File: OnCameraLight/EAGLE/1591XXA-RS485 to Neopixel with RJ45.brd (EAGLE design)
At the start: 54 x 29 mm, 8 parts, among them IC1 75176AP, J1 RJHSE-5381

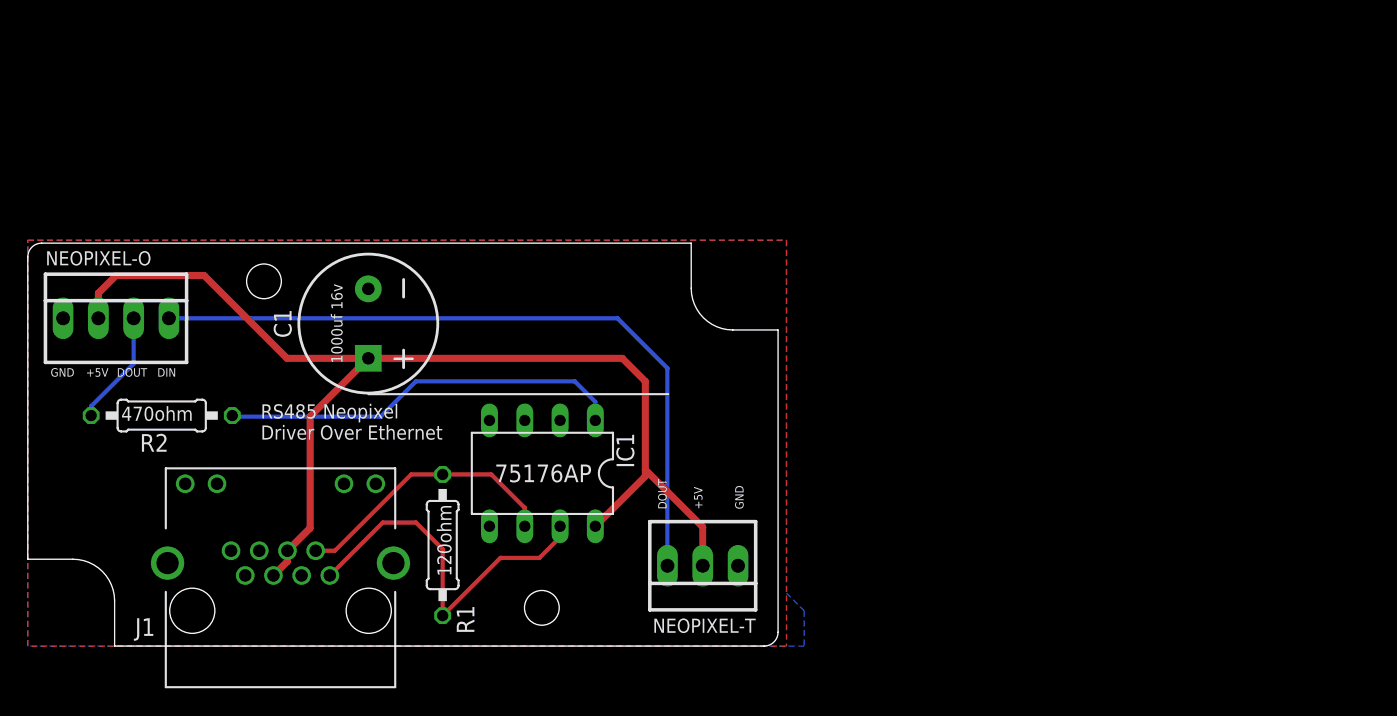
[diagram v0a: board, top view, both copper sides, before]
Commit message: Some more designs to fit different Hammond enclosures.
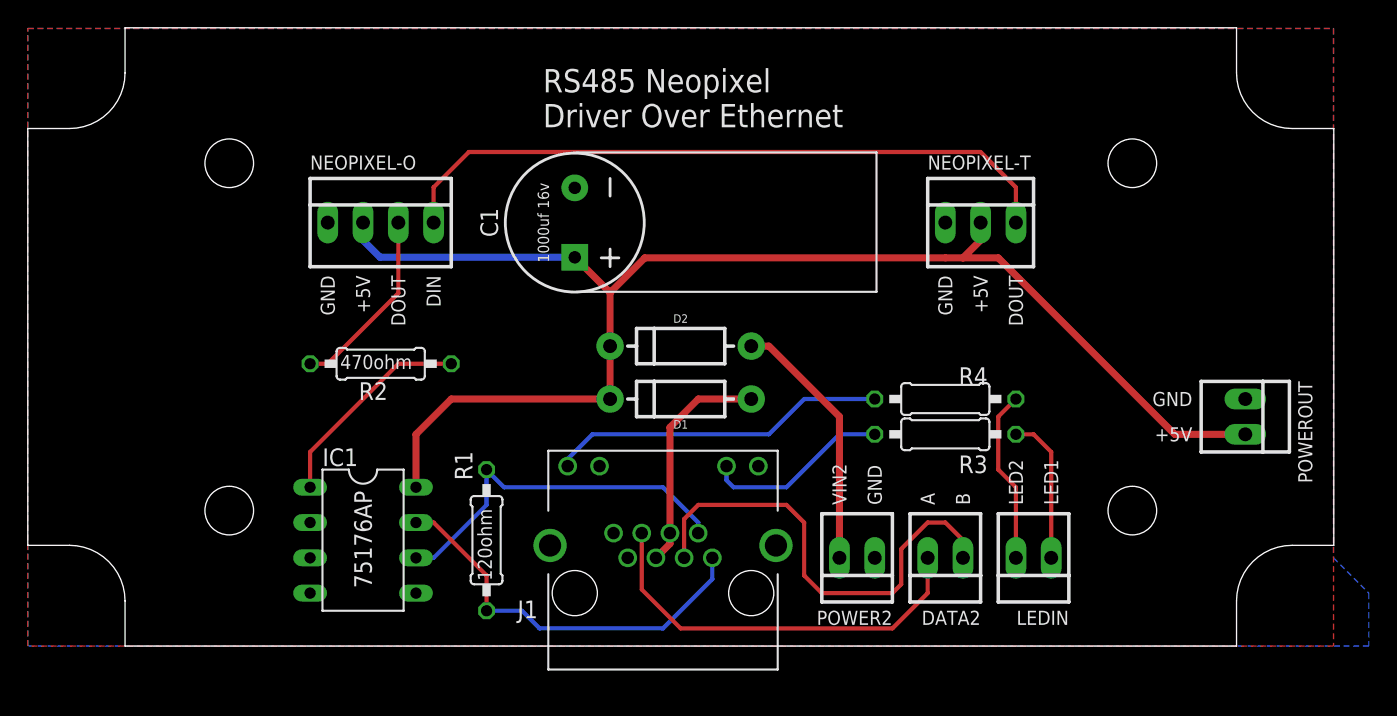
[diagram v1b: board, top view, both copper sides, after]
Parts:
- added D1, D2: 1A/50V/1.1V, SparkFun-DiscreteSemi:DIODE-1N4001
- added DATA2, LEDIN, POWER2, POWEROUT: 22-23-2021, con-molex:22-23-2021
- added R3, R4: (no value), rcl:0207/10
- BOX1: value HAMMOND-BOX-1551H -> HAMMOND-BOX-1591XXA; device hammond:1551H -> hammond:1591XXA
- moved NEOPIXEL-T 31.8 mm to (68.6, 30.5), turned to 0 degrees
- moved J1 27.6 mm to (45.7, 3.81)
- moved NEOPIXEL-O 20.3 mm to (25.4, 30.5)
- moved C1 16.5 mm to (39.4, 30.5)
- moved R2 16.2 mm to (25.4, 20.3)
- moved IC1 13.8 mm to (24.1, 7.62), turned to 270 degrees
- moved R1 3.18 mm to (33.0, 7.62), turned to 270 degrees
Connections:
- removed net DATA2+: J1.3
- removed net DATA2-: J1.6
- removed net RS485+: IC1.7, J1.1, R1.1
- removed net RS485-: IC1.6, J1.2, R1.2
- new net DATA1A: IC1.6, J1.2, R1.1
- new net DATA1B: IC1.7, J1.1, R1.2
- new net DATA2A: DATA2.2, J1.6
- new net DATA2B: DATA2.1, J1.3
- new net LED1IN: LEDIN.1, R3.1
- new net LED2IN: LEDIN.2, R4.1
- new net VIN1: D1.A, J1.4, J1.5
- new net VIN2: D2.A, POWER2.2
- net GND: now also POWER2.1, POWEROUT.1
- net LED1: now also R3.2
- net LED2: now also R4.2
- net VCC: now also D1.C, D2.C, POWEROUT.2; no longer J1.4, J1.5
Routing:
- net DATA2B: track 0.00 -> 33.5 mm
- net DATA2A: track 0.00 -> 29.4 mm
- net DATA1B: track 0.00 -> 29.0 mm
- net RS485+: track 26.8 -> 0.00 mm
- net DATA1A: track 0.00 -> 26.8 mm
- net LED2: track 0.00 -> 24.4 mm
- net RS485-: track 19.6 -> 0.00 mm
- net VIN2: track 0.00 -> 18.6 mm
- net VCC: track 83.9 -> 102.2 mm
- net VIN1: track 0.00 -> 16.5 mm
- net NEODATA: track 29.2 -> 15.3 mm
- net LED1: track 0.00 -> 13.5 mm
- net LED2IN: track 0.00 -> 12.5 mm
- net LED1IN: track 0.00 -> 10.7 mm
- net NEO-O: track 8.27 -> 13.5 mm
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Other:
- board size 54 x 29 mm -> 94 x 44.5 mm
- board text added: "A"
- board text added: "B"
- board text added: "Fits Hammond 1591XXA"
- board text added: "LED1"
- board text added: "LED2"
- board text added: "VIN2"
- board text removed: "Fits Hammond 1551H"

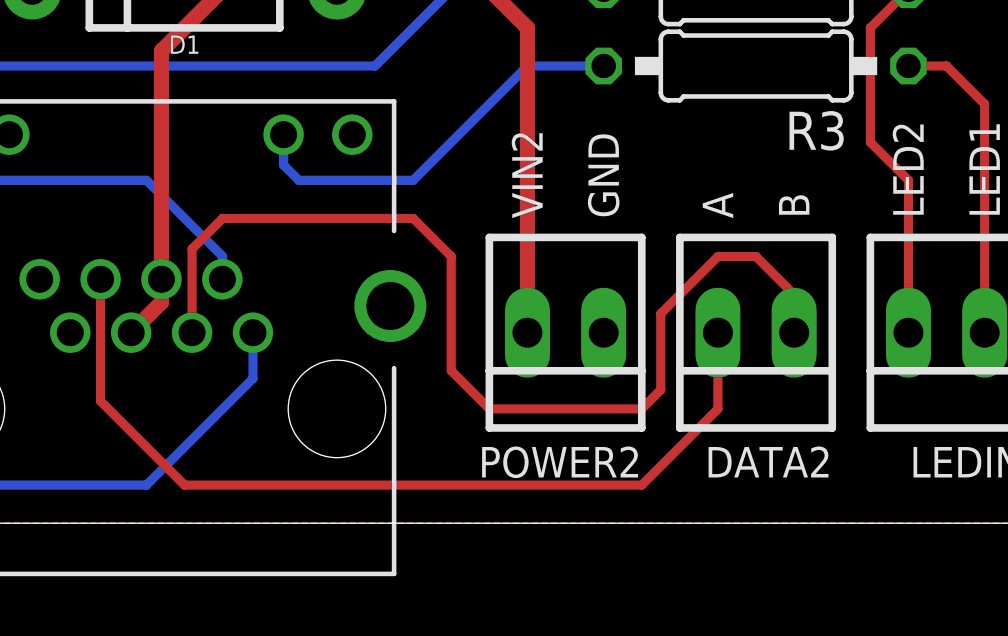
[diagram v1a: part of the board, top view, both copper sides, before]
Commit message: Go through and fix notation on RS485 wiring everywhere to use the standard A/B notation.
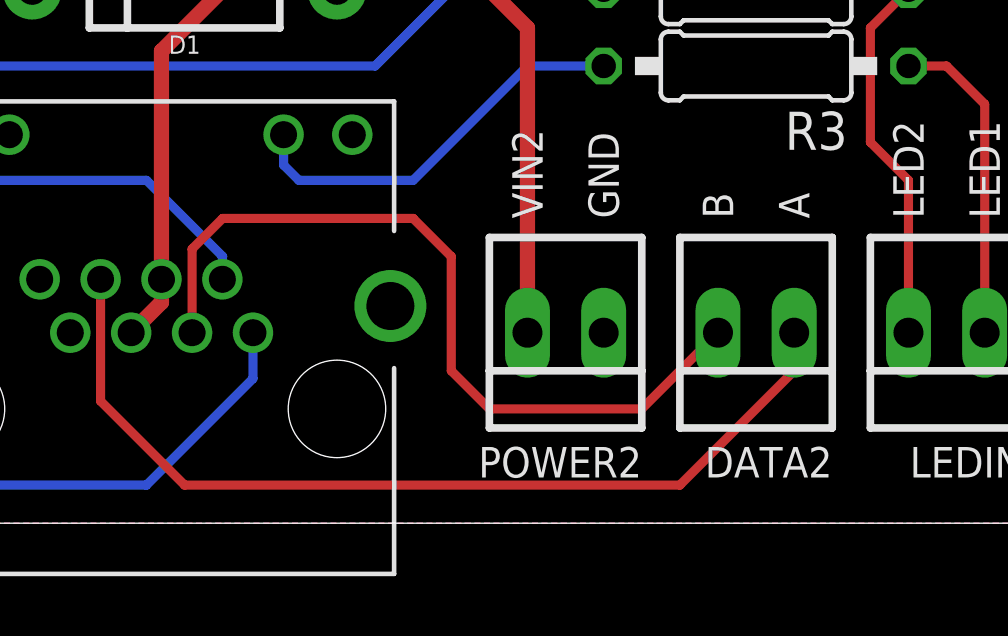
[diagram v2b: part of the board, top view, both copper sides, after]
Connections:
- net DATA2A: now also DATA2.1; no longer DATA2.2
- net DATA2B: now also DATA2.2; no longer DATA2.1
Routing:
- net DATA2B: track 33.5 -> 26.7 mm
- net DATA2A: track 29.4 -> 31.2 mm
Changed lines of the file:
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@@
 <drawing>
 <settings>
-<setting alwaysvectorfont="yes"/>
+<setting alwaysvectorfont="no"/>
 <setting verticaltext="up"/>
 </settings>
@@
 <text x="60.96" y="10.16" size="1.016" layer="25" rot="R90" align="center-left">GND</text>
 <text x="58.42" y="10.16" size="1.016" layer="25" rot="R90" align="center-left">VIN2</text>
-<text x="64.77" y="10.16" size="1.016" layer="25" rot="R90" align="center-left">A</text>
-<text x="67.31" y="10.16" size="1.016" layer="25" rot="R90" align="center-left">B</text>
+<text x="64.77" y="10.16" size="1.016" layer="25" rot="R90" align="center-left">B</text>
+<text x="67.31" y="10.16" size="1.016" layer="25" rot="R90" align="center-left">A</text>
 <text x="71.12" y="10.16" size="1.016" layer="25" rot="R90" align="center-left">LED2</text>
 <text x="73.66" y="10.16" size="1.016" layer="25" rot="R90" align="center-left">LED1</text>
@@
 <signal name="DATA2B">
 <contactref element="J1" pad="3"/>
-<contactref element="DATA2" pad="1"/>
 <wire x1="47.24" y1="6.35" x2="47.24" y2="9.14" width="0.3048" layer="1"/>
 <wire x1="47.24" y1="9.14" x2="48.26" y2="10.16" width="0.3048" layer="1"/>
@@
 <wire x1="55.88" y1="8.89" x2="55.88" y2="5.08" width="0.3048" layer="1"/>
 <wire x1="55.88" y1="5.08" x2="57.15" y2="3.81" width="0.3048" layer="1"/>
-<wire x1="57.15" y1="3.81" x2="62.23" y2="3.81" width="0.3048" layer="1"/>
-<wire x1="62.23" y1="3.81" x2="62.865" y2="4.445" width="0.3048" layer="1"/>
-<wire x1="62.865" y1="4.445" x2="62.865" y2="6.985" width="0.3048" layer="1"/>
-<wire x1="62.865" y1="6.985" x2="64.77" y2="8.89" width="0.3048" layer="1"/>
-<wire x1="64.77" y1="8.89" x2="66.04" y2="8.89" width="0.3048" layer="1"/>
-<wire x1="66.04" y1="8.89" x2="67.31" y2="7.62" width="0.3048" layer="1"/>
-<wire x1="67.31" y1="7.62" x2="67.31" y2="6.35" width="0.3048" layer="1"/>
+<wire x1="62.23" y1="3.81" x2="57.15" y2="3.81" width="0.3048" layer="1"/>
+<contactref element="DATA2" pad="2"/>
+<wire x1="64.77" y1="6.35" x2="62.23" y2="3.81" width="0.3048" layer="1"/>
 </signal>
 <signal name="DATA2A">
 <contactref element="J1" pad="6"/>
-<contactref element="DATA2" pad="2"/>
 <wire x1="44.19" y1="8.13" x2="44.19" y2="4.07" width="0.3048" layer="1"/>
 <wire x1="44.19" y1="4.07" x2="46.99" y2="1.27" width="0.3048" layer="1"/>
-<wire x1="62.23" y1="1.27" x2="64.77" y2="3.81" width="0.3048" layer="1"/>
-<wire x1="64.77" y1="3.81" x2="64.77" y2="6.35" width="0.3048" layer="1"/>
-<wire x1="46.99" y1="1.27" x2="62.23" y2="1.27" width="0.3048" layer="1"/>
+<wire x1="63.5" y1="1.27" x2="67.31" y2="5.08" width="0.3048" layer="1"/>
+<wire x1="46.99" y1="1.27" x2="63.5" y2="1.27" width="0.3048" layer="1"/>
+<contactref element="DATA2" pad="1"/>
+<wire x1="67.31" y1="5.08" x2="67.31" y2="6.35" width="0.3048" layer="1"/>
 </signal>
 </signals>
